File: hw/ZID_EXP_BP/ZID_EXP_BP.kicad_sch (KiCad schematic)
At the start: 47 parts, among them J1 FFC/FPC-40 Socket, J2 Conn_02x05_2.54mm, J3 Conn_02x05_2.54mm, J4 USB-C PWR ONLY, J6 Conn_02x03_Odd_Even, J7 Conn_02x03_Odd_Even, J9 HDR 2x10 Pin, Q1 DMG2305UX, U1 74HCT138

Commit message: PCB: AB+PCL pinout. Exp-BP add position.
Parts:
- removed C1, C?: 47uF, Capacitor_SMD:C_1210_3225Metric_Pad1.33x2.70mm_HandSolder, symbol Device:C_Small
- removed J2, J3: Conn_02x05_2.54mm, symbol Connector_Generic:Conn_02x05_Row_Letter_First
- removed JP1: Jumper_2_Small_Open, symbol Jumper:Jumper_2_Small_Open
- removed OP9: Conn_02x08_2mm, symbol Connector_Generic:Conn_02x08_Row_Letter_First
- removed U1: 74HCT138, symbol 74xx:74HCT138
- added C3, C4: 100UF TANT, Capacitor_Tantalum_SMD:CP_EIA-7343-31_Kemet-D_HandSolder, symbol Device:C_Polarized_US
- added D1: SMAJ6.0A, Diode_SMD:D_SMA, symbol Diode:ESD5Zxx
- added H3: MountingHole, MountingHole:MountingHole_3.2mm_M3, symbol Mechanical:MountingHole
- added J10: Conn 2x02 0.1" pin, Connector_PinHeader_2.54mm:PinHeader_2x02_P2.54mm_Vertical, symbol Connector_Generic:Conn_02x02_Odd_Even
- added J11, J12: Conn 2x04 0.1" pin, Connector_PinHeader_2.54mm:PinHeader_2x04_P2.54mm_Vertical, symbol Connector_Generic:Conn_02x04_Odd_Even
- added J5, J6: Conn 2x02 HDR Pin 2.54mm, symbol Connector_Generic:Conn_02x02_Odd_Even
- added J7: ~, symbol AES_Library:RC2014_BUS_BP80-AES
- added J?: Conn 2x03 HDR Pin 2.54mm, symbol Connector_Generic:Conn_02x03_Odd_Even
- added JP?: Conn 1x02 HDR Pin 2.0mm, symbol Jumper:Jumper_2_Small_Bridged
- added OP?: AES-Option_A-B, Connector_PinHeader_2.54mm:PinHeader_1x03_P2.54mm_Vertical, symbol AES_Library:AES-Option_A-B
- added R? (x3): 47k, Resistor_SMD:R_0805_2012Metric_Pad1.20x1.40mm_HandSolder, symbol Device:R_Small_US
- added U? (x3): 27WZ06, symbol AES_Library:NL27WZ06DFT2G-AES
- added U?: 22V10, symbol AES_Library:ATF750C-DIP24-AES
- added U?: 74AHCT1G32, symbol 74xGxx:74AHCT1G32
- J1: renamed from J5; Function (none) -> RCB-Z80 POS1
- J4: renamed from J8; Function (none) -> RCB-Z80 POS2
- renumbered C7 to C1, C6 to C2, C2 to C5, C3 to C6, C4 to C7, C5 to C8, H6 to H2, H7 to H4, H8 to H5, H2 to H6, H3 to H7, H4 to H8, H5 to H9, J4 to J13, J6 to J2, J7 to J3, J9 to J8, J1 to J9, OP8 to OP1, OP1 to OP2, OP2 to OP3, OP3 to OP4, OP4 to OP5, OP5 to OP6, OP6 to OP8, OP7 to OP9, R2 to R1, R6 to R2, R7 to R3, R8 to R5, R5 to R6, R3 to R7, R1 to R8
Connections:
- net A0: now also J7.16 (A0)
- net A1: now also J7.15 (A1)
- net A10: now also J7.6 (A10)
- net A11: now also J7.5 (A11)
- net A12: now also J7.4 (A12)
- net A13: now also J7.3 (A13)
- net A14: now also J7.2 (A14)
- net A15: now also J7.1 (A15)
- net A16: now also J7.56 (A16)
- net A17: now also J7.55 (A17)
- net A18: now also J7.54 (A18)
- net A19: now also J7.53 (A19)
- net A2: now also J7.14 (A2), U?.5 (IN5)
- net A20: now also J7.52 (A20)
- net A21: now also J7.51 (A21)
- net A22: now also J7.50 (A22)
- net A23: now also J7.49 (A23)
- net A3: now also J7.13 (A3)
- net A4: now also J7.12 (A4)
- net A5: now also J7.11 (A5), U?.6 (IN6)
- net A6: now also J7.10 (A6), U?.7 (IN7)
- net A7: now also J7.9 (A7), U?.8 (IN8)
- net A8: now also J7.8 (A8)
- net A9: now also J7.7 (A9)
- net BACK-: now also J7.62 (~{BSACK})
- net BAI2: now also J5.1 (Pin_1)
- net BAO2: now also J5.4 (Pin_4)
- net BREQ-: now also J7.64 (~{BSREQ})
- net CLK: now also J7.21 (CLK)
- net D0: now also J7.27 (D0), U?.14 (IO1)
- net D1: now also J7.28 (D1), U?.15 (IO2)
- net D10: now also J7.69 (D10)
- net D11: now also J7.70 (D11)
- net D12: now also J7.71 (D12)
- net D13: now also J7.72 (D13)
- net D14: now also J7.73 (D14)
- net D15: now also J7.74 (D15)
- net D2: now also J7.29 (D2), U?.16 (IO3)
- net D3: now also J7.30 (D3), U?.17 (IO4)
- net D4: now also J7.31 (D4), U?.18 (IO5)
- net D5: now also J7.32 (D5), U?.19 (IO6)
- net D6: now also J7.33 (D6), U?.20 (IO7)
- net D7: now also J7.34 (D7), U?.21 (IO8)
- net D8: now also J7.67 (D8)
- net D9: now also J7.68 (D9)
- net DISPSEL-: now also U?.23 (IO10)
- net DSPBLON-: now also OP2.1 (A); no longer OP5.1 (A)
- net FONT1: now also OP3.1 (A); no longer OP4.1 (A)
- net GND: now also C3.2, C4.2, D1.2 (A), J11.1 (Pin_1), J11.3 (Pin_3), J11.5 (Pin_5), J11.7 (Pin_7), J12.1 (Pin_1), J12.3 (Pin_3), J12.5 (Pin_5), J7.17 (GND), J7.57 (GND), J?.1 (Pin_1), J?.3 (Pin_3), J?.5 (Pin_5), U?.12 (GND), U?.2 (GND), U?.3 (GND)
- net HALT-: now also J7.63 (~{HALT})
- net IEI2: now also J6.1 (Pin_1), J7.38 (IEI)
- net IEO2: now also J6.4 (Pin_4), J7.39 (IEO)
- net INT-: now also J7.22 (~{INT}), JP?.2 (B)
- net IORQ-: now also J7.26 (~{IORQ}), U?.3 (IN3)
- net M1-: now also J7.19 (~{M1})
- net MODINT-: now also J12.8 (Pin_8)
- net MREQ-: now also J7.23 (~{MREQ})
- net NMI-: now also J7.66 (~{NMI})
- net P41: now also J7.41 (P41)
- net P44: now also J7.44 (P44)
- net P45: now also J7.45 (P45)
- net P46: now also J7.46 (P46)
- net P47: now also J7.47 (P47)
- net P48: now also J7.48 (P48)
- net P60: now also J7.60 (PAGE)
- net P61: now also J7.61 (CLK2)
- net RD-: now also J7.25 (~{RD}), U?.4 (IN4)
- net RFSH-: now also J7.59 (~{RFSH})
- net RST-: now also J7.20 (~{RESET})
- net RX: now also J7.36 (RX); no longer OP2.3 (B)
- net RX2: now also J7.76 (RX2); no longer OP8.1 (A)
- net SBC_I0: now also J12.2 (Pin_2)
- net SBC_I1: now also J12.4 (Pin_4), OP?.2 (C)
- net SBC_I2: now also J12.6 (Pin_6)
- net SBC_O0: now also J11.2 (Pin_2)
- net SBC_O1: now also J11.4 (Pin_4)
- net SBC_O2: now also J11.6 (Pin_6)
- net SBC_O3: now also J11.8 (Pin_8)
- net TX: now also OP5.1 (A), J7.35 (TX); no longer OP2.1 (A), OP6.3 (B)
- net TX2: now also J7.75 (TX2); no longer OP8.3 (B)
- net USR4: now also OP2.3 (B), J7.40 (USR4), OP?.3 (B); no longer OP3.1 (A)
- net USR6: now also J7.78 (USR6)
- net USR7: now also OP6.3 (B), J7.79 (USR7)
- net USR8: now also J7.80 (USR8), OP?.1 (A)
- net WAIT-: now also J7.65 (~{WAIT})
- net WR-: now also J7.24 (~{WR})
- net ZINT2: now also J7.77 (~{zINT2})
- net ZIRQ1: now also J7.37 (~{zIRQ1})
- net +5P renamed +5V
- net +5V: now also J7.18 (5V), J7.58 (5V), R?.2, R?.2, R?.2, U?.24 (PWR), U?.5 (VCC), U?.5 (VCC)
- net PWR renamed ZIDPWR
- net ZIDPWR: now also C3.1, J10.1 (Pin_1), J10.2 (Pin_2), J10.3 (Pin_3), J10.4 (Pin_4), J12.7 (Pin_7)
- net VBUS renamed VBUSPWR
- net VBUSPWR: now also C4.1, D1.1 (K)
- new net: J?.2 (Pin_2), R?.1, U?.9 (IN9)
- new net: J?.4 (Pin_4), R?.1, U?.10 (IN10)
- new net: J?.6 (Pin_6), R?.1, U?.11 (IN11)
- new net: JP?.1 (A), U?.6
- new net: U?.3, U?.4
- new net BAI3: J5.2 (Pin_2), J7.42 (BAI)
- new net BAO3: J5.3 (Pin_3), J7.43 (BAO)
- new net IEI3: J6.2 (Pin_2)
- new net IEO: OP8.3 (B)
- new net IEO3: J6.3 (Pin_3)
- new net KBCLR: OP4.1 (A), U?.1, U?.13 (IN12)
- new net KBDATA: U?.2 (IN2), U?.4
- new net KBDCLK: U?.1 (I/CLK)
- new net KBDRDY: OP8.1 (A), U?.1, U?.2, U?.22 (IO9)
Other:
- moved on the sheet: C1, C2, C5, C6, C7, C8, DISP1, H4, H5, H6, H7, H8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

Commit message: PCB layout progress before SRAM move. PLD: Allow upper-8 address only on BRK1.
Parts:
- removed C3: 100UF TANT, Capacitor_Tantalum_SMD:CP_EIA-7343-31_Kemet-D_HandSolder, symbol Device:C_Polarized_US
- removed J?: Conn 2x03 HDR Pin 2.54mm, symbol Connector_Generic:Conn_02x03_Odd_Even
- removed JP?: Conn 1x02 HDR Pin 2.0mm, symbol Jumper:Jumper_2_Small_Bridged
- removed R? (x3): 47k, Resistor_SMD:R_0805_2012Metric_Pad1.20x1.40mm_HandSolder, symbol Device:R_Small_US
- removed U? (x3): 27WZ06, symbol AES_Library:NL27WZ06DFT2G-AES
- removed U?: 22V10, symbol AES_Library:ATF750C-DIP24-AES
- removed U?: 74AHCT1G32, symbol 74xGxx:74AHCT1G32
- added J13: RJ9, symbol Connector:RJ9
- added J15: JST-PH-K B6B, Connector_JST:JST_PH_B6B-PH-K_1x06_P2.00mm_Vertical, symbol Connector_Generic:Conn_01x06
- added JP1: Conn 1x02 HDR Pin 2.0mm, symbol Jumper:Jumper_2_Small_Bridged
- added R10, R8, R9: 4.7k, Resistor_SMD:R_0805_2012Metric, symbol Device:R_Small_US
- added R4, R5: 10k, Resistor_SMD:R_0805_2012Metric_Pad1.20x1.40mm_HandSolder, symbol Device:R_Small_US
- added R7: 10k, Resistor_SMD:R_0805_2012Metric, symbol Device:R_Small_US
- added RN1: 100k, Resistor_THT:R_Array_SIP9, symbol Device:R_Network08_US
- added SW1: SW_DIP_x08, symbol Switch:SW_DIP_x08
- added U1: ATF1502AS-44T, Package_QFP:TQFP-44_10x10mm_P0.8mm, symbol AES_Library:ATF1502AS-44T-AES
- gave numbers to parts that had none: 1
- renumbered C4 to C2, C5 to C3, C6 to C4, C7 to C5, C8 to C6, C2 to C7, C1 to C8, H6 to H4, H7 to H5, H8 to H6, H9 to H7, H4 to H8, H5 to H9, J9 to J1, J5 to J10, J6 to J11, J7 to J12, J8 to J14, J11 to J2, J10 to J3, J12 to J4, J1 to J5, J2 to J6, J3 to J7, J13 to J8, J4 to J9, R6 to R11, R2 to R12, R3 to R13, R5 to R14, R8 to R2, R7 to R3, R4 to R6
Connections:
- net IEO is gone; now on net USR4: OP8.3 (B)
- net KBCLR is gone; now on net TX2: OP4.1 (A)
- net +5V: now also C2.1, D1.1 (K), J13.4, J15.4 (Pin_4), R10.1, R4.2, R5.2, R7.1, R8.1, R9.1, RN1.1 (common), U1.17 (VCCINT), U1.29 (VCCINT), U1.41 (VCCINT), U1.9 (VCCINT)
- net A1: now also U1.28 (BMC23/IO)
- net A2: now also U1.30 (BMC22/IO)
- net A3: now also U1.31 (BMC21/IO)
- net A4: now also U1.33 (BMC19/IO)
- net A5: now also U1.34 (BMC18/IO)
- net A6: now also U1.42 (AMC1/IO)
- net A7: now also U1.43 (AMC2/IO)
- net D0: now also U1.19 (B31/IO/PD2)
- net D1: now also U1.15 (AMC16/IO)
- net D2: now also U1.14 (AMC15/IO)
- net D3: now also U1.11 (AMC12/IO)
- net D4: now also U1.10 (AMC11/IO)
- net D5: now also U1.8 (AMC10/IO)
- net D6: now also U1.6 (AMC8/IO)
- net D7: now also U1.2 (AMC5/IO)
- net DISPSEL-: now also U1.44 (AMC3/IO)
- net DSPBLON-: now also U1.3 (AMC6/IO); no longer OP2.1 (A)
- net FONT1: now also U1.12 (AMC13/IO); no longer OP3.1 (A)
- net GND: now also J13.1, J15.2 (Pin_2), SW1.1, SW1.2, SW1.3, SW1.4, SW1.5, SW1.6, SW1.7, SW1.8, U1.16 (GND), U1.24 (GND), U1.36 (GND), U1.4 (GND); no longer J2.1 (Pin_1), J2.3 (Pin_3), J2.5 (Pin_5), J2.7 (Pin_7)
- net IEI2: no longer J12.38 (IEI)
- net IEI3: now also J12.38 (IEI)
- net IEO2: no longer J12.39 (IEO)
- net IEO3: now also J12.39 (IEO)
- net INT-: now also JP1.2 (B)
- net IORQ-: now also U1.40 (IN/OE2/GCK2)
- net KBDATA: now also J13.2, R4.1, U1.20 (BMC30/IO), U1.5 (A7/IO/PD1)
- net KBDCLK: now also J13.3, R5.1, U1.13 (AMC14/IO), U1.37 (IN/GCK1)
- net KBDRDY: now also JP1.1 (A), U1.18 (BMC32/IO); no longer OP8.1 (A)
- net RD-: now also U1.38 (IN/OE1)
- net RST-: now also U1.39 (IN/GCLR)
- net RX: now also OP3.1 (A); no longer OP6.1 (A)
- net RX2: now also OP5.1 (A)
- net TX: now also OP2.1 (A); no longer OP5.1 (A)
- net USR4: now also OP4.3 (B); no longer OP2.3 (B), OP7.3 (B)
- net USR6: now also OP2.3 (B), OP6.3 (B); no longer OP3.3 (B)
- net USR7: now also OP3.3 (B), OP7.3 (B); no longer OP4.3 (B), OP6.3 (B)
- net USR8: no longer OP7.1 (A)
- net VBUSPWR: no longer C2.1, D1.1 (K)
- net WR-: now also U1.35 (B17/IO/GCK3)
- new net: J2.1 (Pin_1), J2.3 (Pin_3), J2.5 (Pin_5), J2.7 (Pin_7)
- new net ASEL3: RN1.5 (R4), SW1.13, U1.21 (BMC29/IO)
- new net ASEL4: RN1.6 (R5), SW1.12, U1.22 (BMC28/IO)
- new net ASEL5: RN1.7 (R6), SW1.11, U1.23 (BMC27/IO)
- new net ASEL6: RN1.8 (R7), SW1.10, U1.25 (BMC26/IO)
- new net ASEL7: RN1.9 (R8), SW1.9, U1.27 (BMC24/IO)
- new net JTCK: J15.1 (Pin_1), R8.2, U1.26 (B25/IO/JT.TCK)
- new net JTDI_CO: J15.6 (Pin_6), R10.2, U1.1 (A4/IO/JT.TDI)
- new net JTDO_CI: J15.3 (Pin_3), R7.2, U1.32 (B20/IO/JT.TDO)
- new net JTMS: J15.5 (Pin_5), R9.2, U1.7 (A9/IO/JT.TMS)
- new net SBCI0: OP6.1 (A), RN1.2 (R1), SW1.16
- new net SBCI1: OP7.1 (A), RN1.3 (R2), SW1.15
- new net SBCI2: OP8.1 (A), RN1.4 (R3), SW1.14
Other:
- moved on the sheet: C2, C3, C4, C5, C6, C7, C8, D1, DISP1, H1, H2, H3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

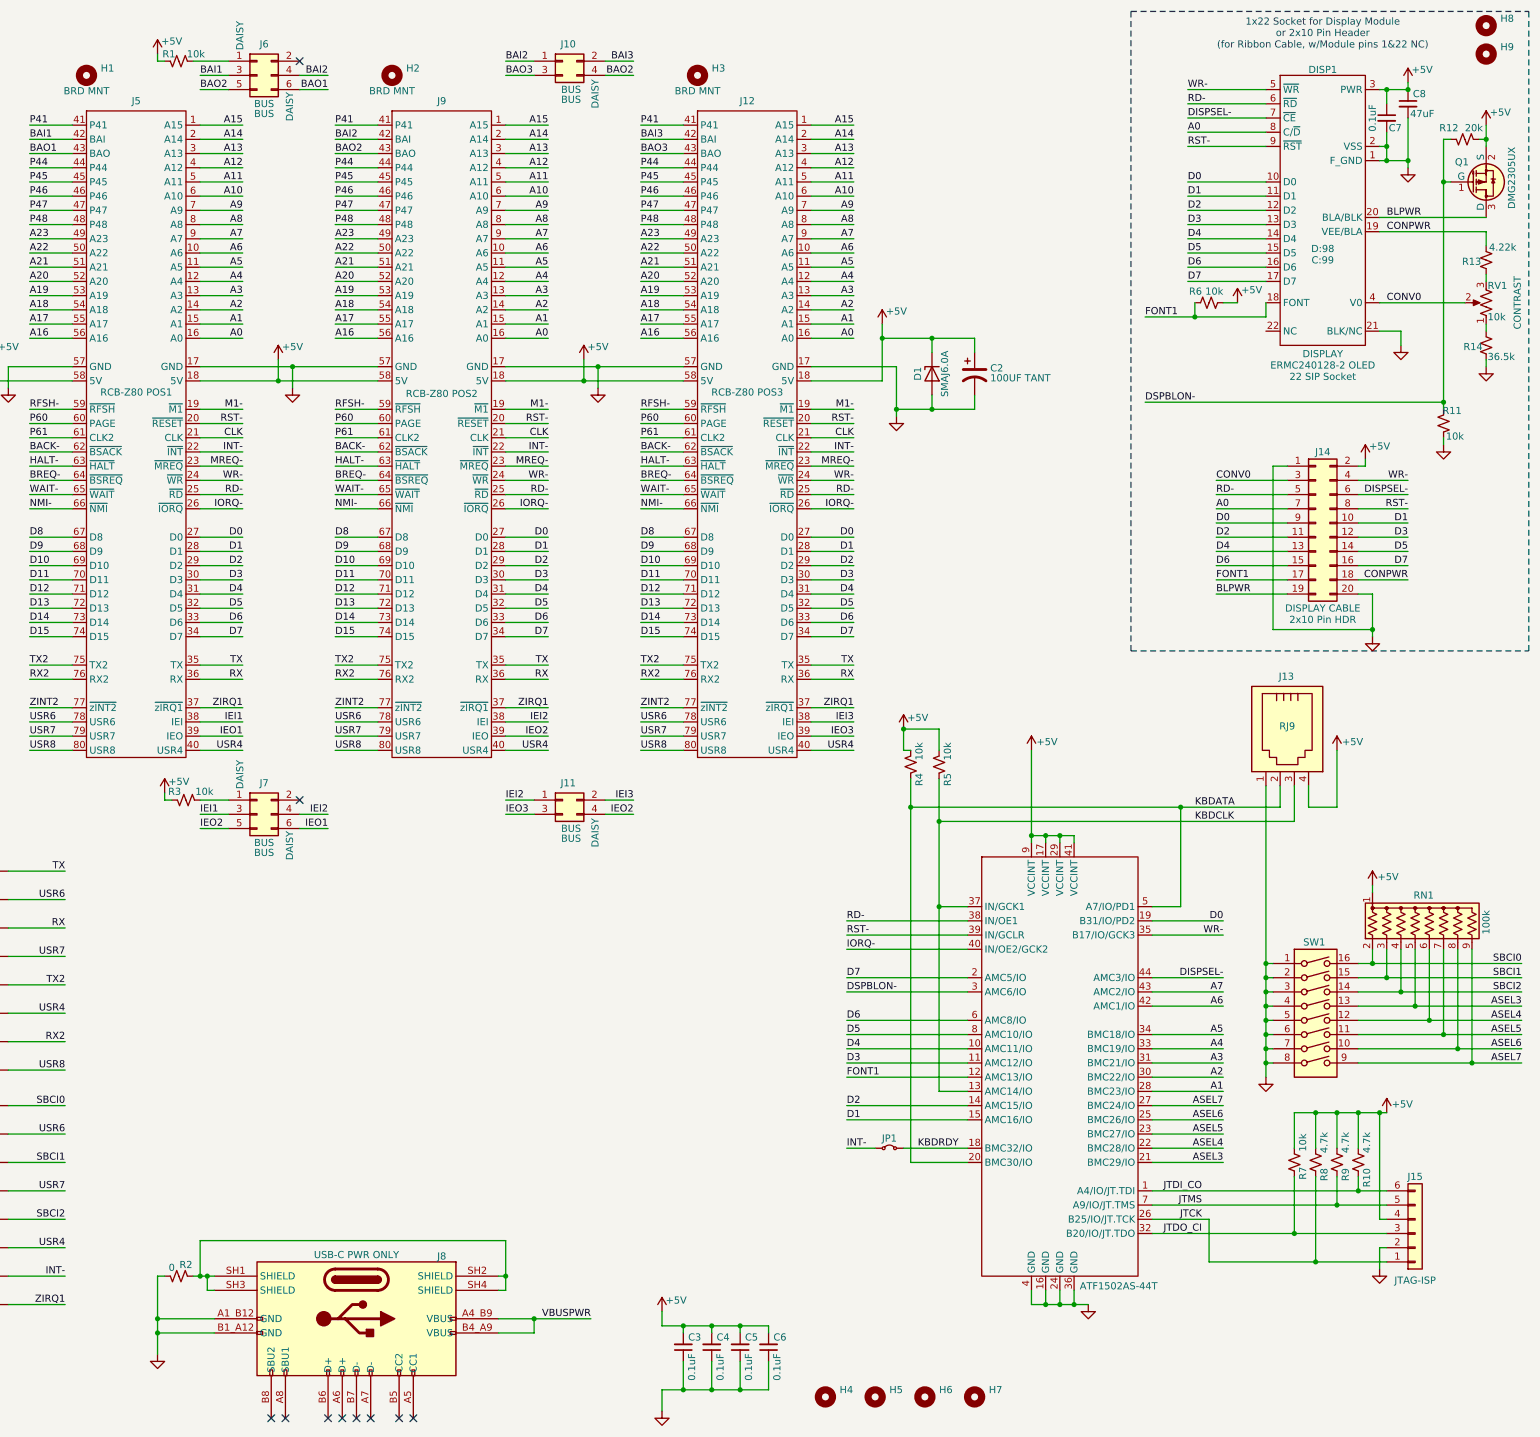
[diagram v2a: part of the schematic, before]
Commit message: Checkpoint before removing JTAG-ISP Chain header (J15)
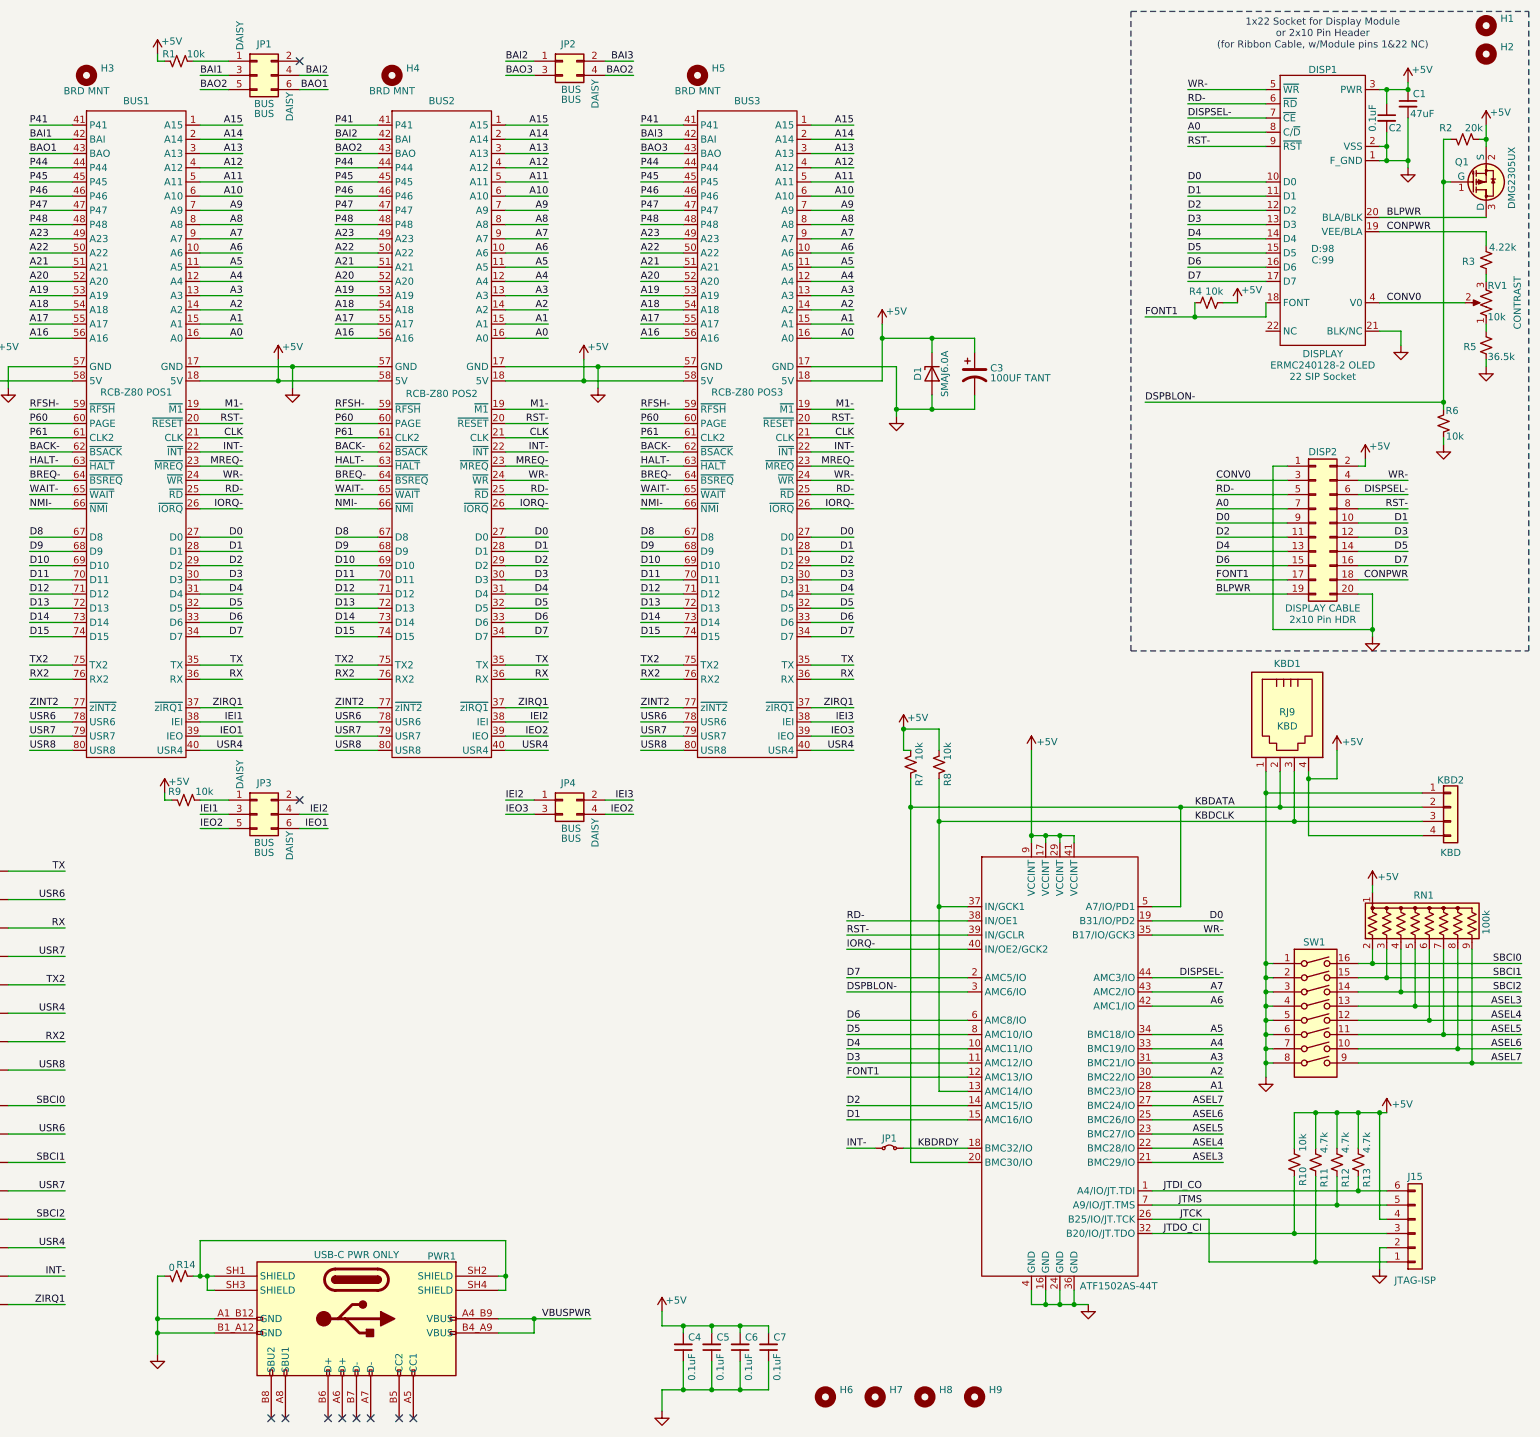
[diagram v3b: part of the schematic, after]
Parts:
- added KBD2: Conn 01x04 Pin hdr 0.1in, symbol Connector_Generic:Conn_01x04
- KBD1: renamed from J13; Function (none) -> KBD; P1 (none) -> GND; P2 (none) -> D; P3 (none) -> C; P4 (none) -> 5V
- renumbered J5 to BUS1, J9 to BUS2, J12 to BUS3, C8 to C1, C7 to C2, C2 to C3, C3 to C4, C4 to C5, C5 to C6, C6 to C7, J14 to DISP2, H8 to H1, H9 to H2, H1 to H3, H2 to H4, H3 to H5, H4 to H6, H5 to H7, H6 to H8, H7 to H9, J6 to JP1, J10 to JP2, J7 to JP3, J11 to JP4, J8 to PWR1, R7 to R10, R8 to R11, R9 to R12, R10 to R13, R2 to R14, R12 to R2, R13 to R3, R6 to R4, R14 to R5, R11 to R6, R4 to R7, R5 to R8, R3 to R9
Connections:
- net +5V: now also KBD2.4 (Pin_4)
- net GND: now also KBD2.1 (Pin_1)
- net KBDATA: now also KBD2.2 (Pin_2)
- net KBDCLK: now also KBD2.3 (Pin_3)
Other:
- moved on the sheet: KBD1
